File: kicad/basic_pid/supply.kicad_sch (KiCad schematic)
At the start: 0 parts

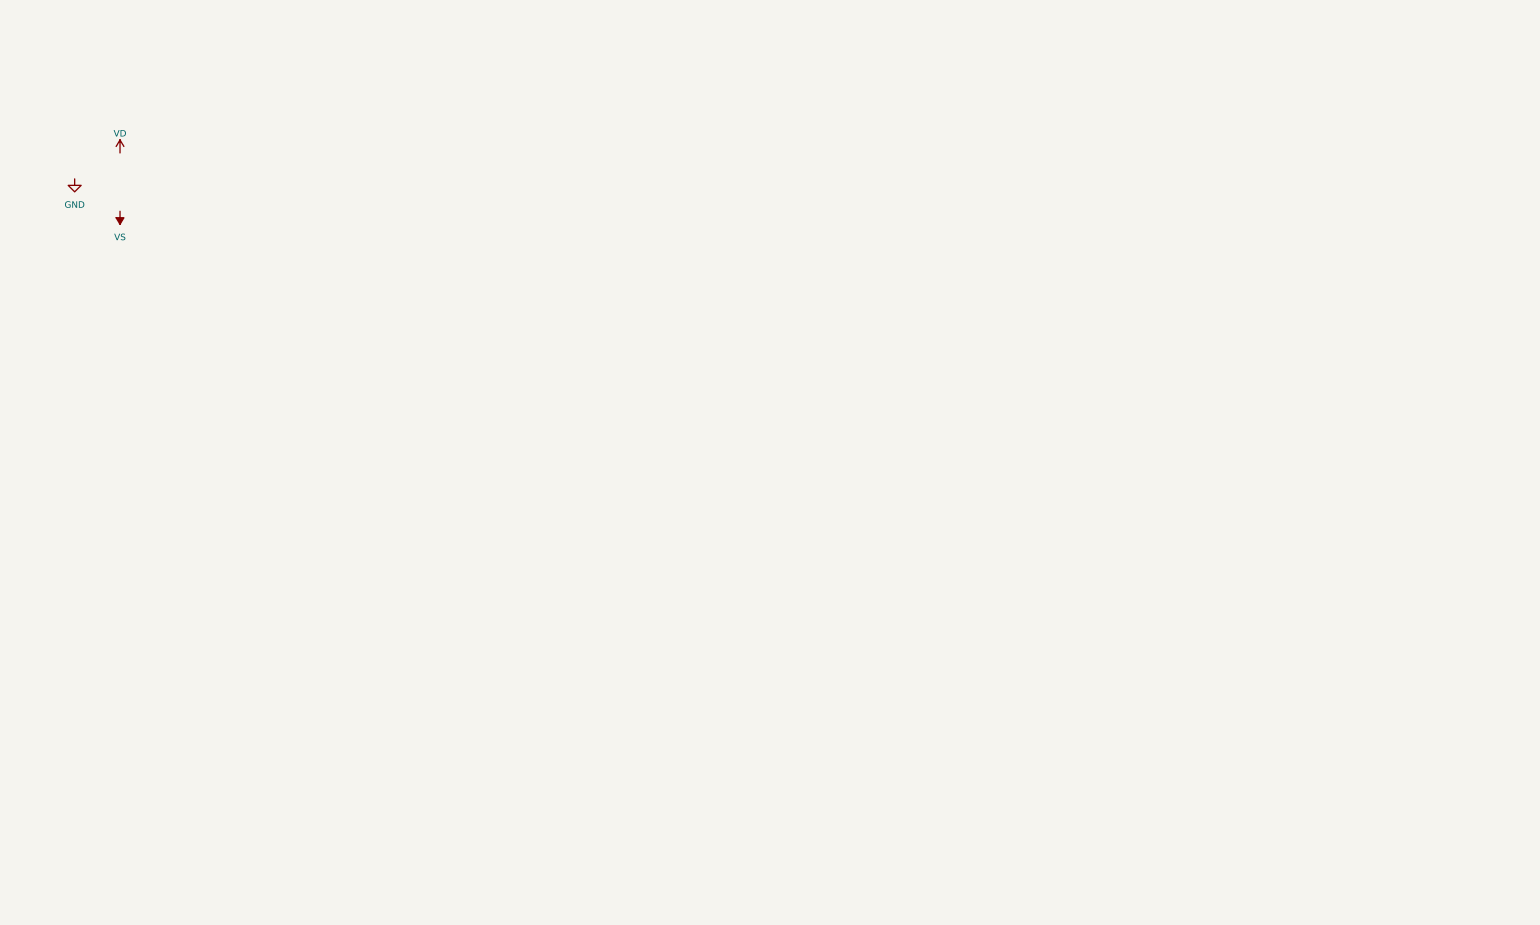
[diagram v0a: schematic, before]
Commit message: Schematic almost finalized:
Ended up using switches to select pre-set capacitors rather than ZIFs

TO DO:
1) design the power supply and filtering section.
2) Layout work (consider adding capacitors for stabilization...)
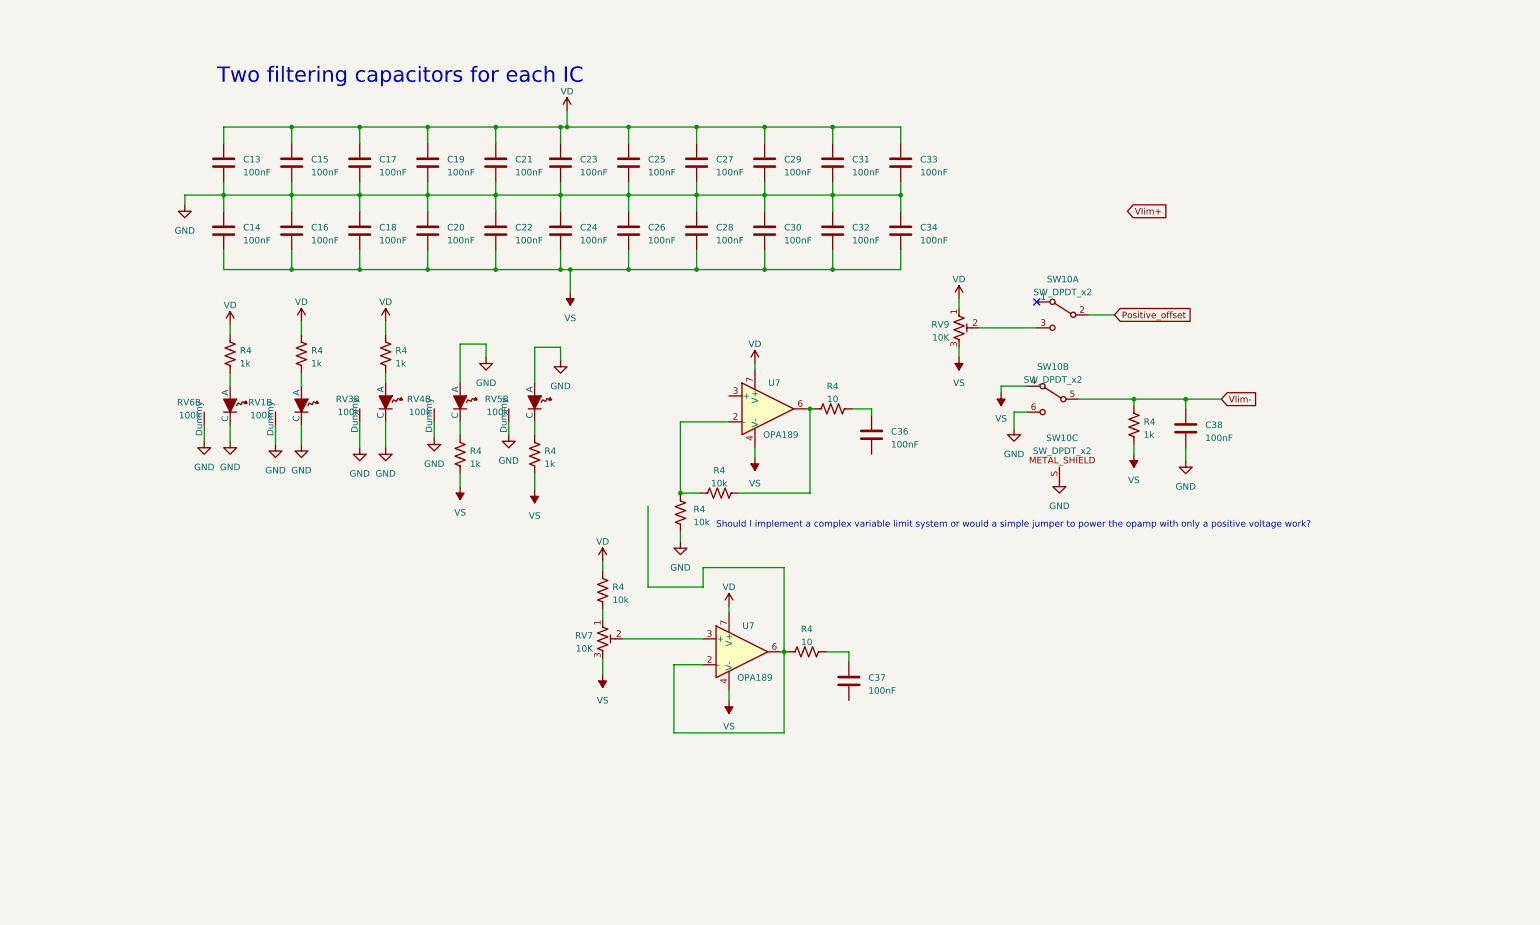
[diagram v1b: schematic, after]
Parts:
- added C13, C14, C15, C16, C17, C18, C19, C20, C21, C22, C23, C24, C25, C26, C27, C28, C29, C30, C31, C32, C33, C34, C36, C37, C38: 100nF, Capacitor_SMD:C_0805_2012Metric, symbol Device:C
- added R4 (x6): 1k, Resistor_SMD:R_0805_2012Metric, symbol Device:R_US
- added R4 (x2): 10, Resistor_SMD:R_0805_2012Metric, symbol Device:R_US
- added R4 (x3): 10k, Resistor_SMD:R_0805_2012Metric, symbol Device:R_US
- added RV1, RV3, RV4, RV5, RV6: 100k, lib:Slide_pot_45mm, symbol local_lib:potentiometer_and _LED
- added RV7, RV9: 10K, Potentiometer_THT:Potentiometer_Bourns_3296W_Vertical, symbol Device:R_Potentiometer_Trim_US
- added SW10: SW_DPDT_x2, lib:MHS222, symbol local_lib:SW_DPDT_x2
- added U7 (x2): OPA189, Package_SO:SOIC-8_3.9x4.9mm_P1.27mm, symbol Amplifier_Operational:OPA330xxD
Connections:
- net GND: now also C13.2, C14.1, C15.2, C16.1, C17.2, C18.1, C19.2, C20.1, C21.2, C22.1, C23.2, C24.1, C25.2, C26.1, C27.2, C28.1, C29.2, C30.1, C31.2, C32.1, C33.2, C34.1, C38.2, R4.2, RV1.C, RV1.L (Dummy), RV3.C, RV3.L (Dummy), RV4.A, RV4.L (Dummy), RV5.A, RV5.L (Dummy), RV6.C, RV6.L (Dummy), SW10.6 (C), SW10.S
- net VD: now also C13.1, C15.1, C17.1, C19.1, C21.1, C23.1, C25.1, C27.1, C29.1, C31.1, C33.1, R4.1, R4.2, R4.2, R4.2, RV9.1, U7.7 (V+), U7.7 (V+)
- net VS: now also C14.2, C16.2, C18.2, C20.2, C22.2, C24.2, C26.2, C28.2, C30.2, C32.2, C34.2, R4.1, R4.1, R4.1, RV7.3, RV9.3, SW10.4 (A), U7.4 (V-), U7.4 (V-)
- new net: R4.1, RV6.A
- new net: R4.2, U7.2 (-), U7.6
- new net: RV7.2, U7.3 (+)
- new net: C36.1, R4.1
- new net: R4.1, R4.2, U7.6
- new net: R4.2, RV7.1
- new net: R4.1, R4.2, U7.2 (-)
- new net: R4.2, RV4.C
- new net: R4.1, RV3.A
- new net: RV9.2, SW10.3 (C)
- new net: C37.1, R4.1
- new net: R4.1, RV1.A
- new net: R4.2, RV5.C
- new net Positive_offset: SW10.2 (B)
- new net Vlim-: C38.1, R4.2, SW10.5 (B)
- no-connect marks 0 -> 1
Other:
- note added: "Should I implement a complex variable limit system or would a simple jumper to power the opamp with only a positive voltage work?"
- note added: "Two filtering capacitors for each IC"

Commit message: last partial schematic using OPA189 everywhere
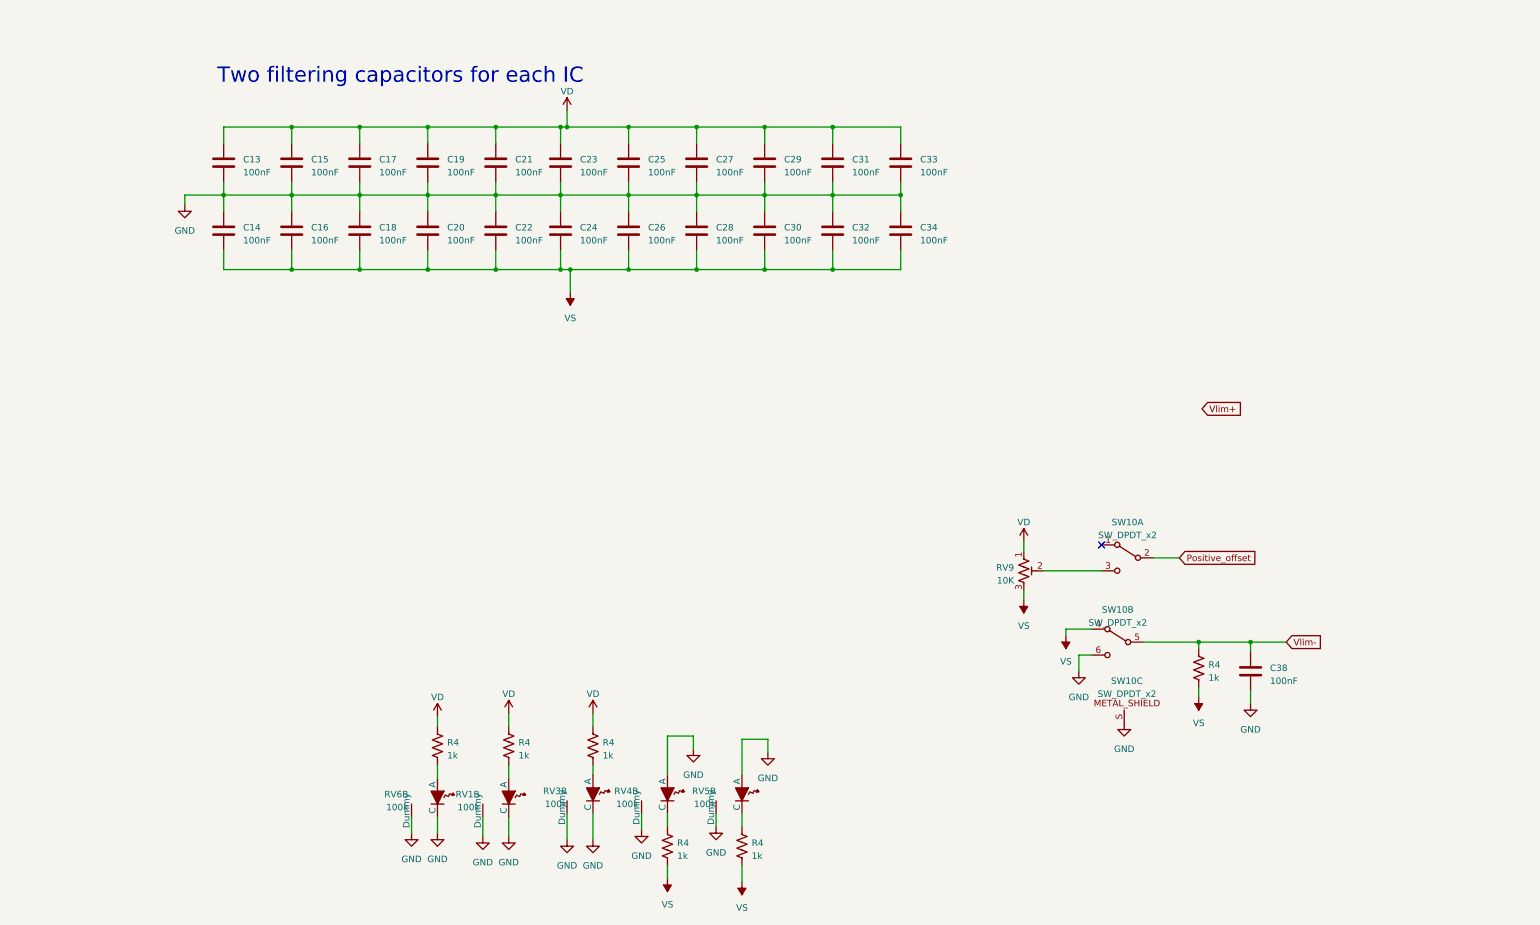
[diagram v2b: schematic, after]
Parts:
- removed C36, C37: 100nF, Capacitor_SMD:C_0805_2012Metric, symbol Device:C
- removed R4 (x2): 10, Resistor_SMD:R_0805_2012Metric, symbol Device:R_US
- removed R4 (x3): 10k, Resistor_SMD:R_0805_2012Metric, symbol Device:R_US
- removed RV7: 10K, Potentiometer_THT:Potentiometer_Bourns_3296W_Vertical, symbol Device:R_Potentiometer_Trim_US
- removed U7 (x2): OPA189, Package_SO:SOIC-8_3.9x4.9mm_P1.27mm, symbol Amplifier_Operational:OPA330xxD
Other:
- note removed: "Should I implement a complex variable limit system or would a simple jumper to power the opamp with only a positive voltage work?"
- moved on the sheet: C38, R4, RV1B, RV3B, RV4B, RV5B, RV6B, RV9, SW10A, SW10B, SW10C

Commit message: Schematic finalized and layout work begun
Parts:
- added C18, C19: 22mF, Capacitor_THT:CP_Radial_D30.0mm_P10.00mm_SnapIn, symbol Device:C_Polarized
- added C24, C25, C42: 10uF, Capacitor_SMD:C_1210_3225Metric, symbol Device:C
- added C32, C33: 220uF, Capacitor_SMD:CP_Elec_8x6.9, symbol Device:C_Polarized
- added C44: 22uF, Capacitor_SMD:CP_Elec_4x5.8, symbol Device:C_Polarized
- added D1: GBU4A, Diode_THT:Diode_Bridge_Vishay_GBU, symbol Diode_Bridge:GBU4A
- added H1, H2, H3, H4: MountingHole, MountingHole:MountingHole_3.2mm_M3_ISO14580, symbol Mechanical:MountingHole
- added J5: Screw_Terminal_01x04, TerminalBlock:TerminalBlock_Altech_AK300-4_P5.00mm, symbol Connector:Screw_Terminal_01x04
- added J6: Screw_Terminal_01x03, TerminalBlock:TerminalBlock_Altech_AK300-3_P5.00mm, symbol Connector:Screw_Terminal_01x03
- added R4: DNP, Resistor_SMD:R_0805_2012Metric, symbol Device:R_US
- added R4: 1k, Resistor_SMD:R_0805_2012Metric, symbol Device:R_US
- added R4: 330, Resistor_SMD:R_0805_2012Metric, symbol Device:R_US
- added RV7: 2k, Potentiometer_THT:Potentiometer_Bourns_3296W_Vertical, symbol Device:R_Potentiometer_Trim_US
- added SW1, SW2, SW3, SW5: SW_DPDT_x2, lib:MHS222, symbol local_lib:SW_DPDT_x2
- added U14: LM2940CS-12/NOPB, Package_TO_SOT_SMD:TO-263-3_TabPin2, symbol Regulator_Linear:LM2937xS
- added U15: LM2990SX-12, Package_TO_SOT_SMD:TO-263-3_TabPin2, symbol Regulator_Linear:LM2990SX-12
- added U16: LM317_TO-252, Package_TO_SOT_SMD:TO-252-2, symbol Regulator_Linear:LM317_TO-252
- RV6: renamed from RV9; DIGIKEY (none) -> 118-3296W-1-103RLFCT-ND; PARTNO (none) -> 3296W-1-103RLF
- renumbered C13 to C14, C14 to C15, C15 to C16, C16 to C17, C17 to C20, C18 to C21, C19 to C22, C20 to C23, C21 to C26, C22 to C27, C23 to C28, C24 to C29, C25 to C30, C26 to C31, C27 to C34, C28 to C35, C29 to C36, C30 to C37, C31 to C38, C32 to C39, C33 to C40, C34 to C41, C38 to C43
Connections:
- net GND: now also RV6.1, C18.2, C19.1, C24.2, C25.1, C32.2, C33.1, C42.2, C44.2, J5.2 (Pin_2), J5.3 (Pin_3), J6.2 (Pin_2), RV7.2, RV7.3, SW1.S, SW2.S, SW3.S, SW5.S, U14.2 (GND), U15.1 (GND)
- net Vlim+: now also C44.1, R4.2, U16.2 (VO)
- net at RV6.2, SW10.3 (C): now also R4.2
- net VD renamed +12V
- net +12V: now also C32.1, U14.3 (VO); no longer RV6.1
- net VS renamed -12V
- net -12V: now also C33.2, R4.1, U15.3 (OUT)
- new net: C19.2, C25.2, D1.4 (-), J6.3 (Pin_3), U15.2 (IN)
- new net: D1.3, J5.1 (Pin_1)
- new net: D1.2, J5.4 (Pin_4)
- new net: R4.1, RV7.1
- new net: R4.1, R4.2, U16.1 (ADJ)
- new net V+_unreg: C18.1, C24.1, C42.1, D1.1 (+), J6.1 (Pin_1), U14.1 (VI), U16.3 (VI)
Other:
- note added: "Additional parts: 237-1326-ND VPT30-830 (toroidal transformer) 1144-1033-ND 06AE2 (Power Entry Module)"
- moved on the sheet: C43, R4, RV1B, RV3B, RV6, RV6B, SW10A, SW10B, SW10C

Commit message: Layout almost completed
This is an almost completed snapshot of the layout. Here what to do:

1) Make sure that when flipped the back has sliders on the bottom: this will require
   reversing the direction of increasing gain with consequent shortening of certain
   signal traces

2) Fix the position of connectors, sliders and switches to "reasonable locations"
3) Make a verbose silkscreen (expecially on bottom) showing all functions.
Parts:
- removed C41: 100nF, Capacitor_SMD:C_0805_2012Metric, symbol Device:C
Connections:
- net +12V: no longer C40.1
- net V+_unreg: now also J6.3 (Pin_3); no longer J6.1 (Pin_1)
- net Vlim+: now also C40.1
- net at C19.2, C25.2, D1.4 (-)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: now also J6.1 (Pin_1); no longer J6.3 (Pin_3)
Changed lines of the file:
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@@
   (junction (at 109.22 66.04) (diameter 0) (color 0 0 0 0)
   )
-  (junction (at 175.26 38.1) (diameter 0) (color 0 0 0 0)
-  )
   (junction (at 223.52 88.265) (diameter 0) (color 0 0 0 0)
   )
@@
   (junction (at 211.455 74.295) (diameter 0) (color 0 0 0 0)
   )
-  (junction (at 175.26 66.04) (diameter 0) (color 0 0 0 0)
-  )
   (junction (at 78.105 110.49) (diameter 0) (color 0 0 0 0)
   )
+  (junction (at 257.81 74.295) (diameter 0) (color 0 0 0 0)
+  )
   (junction (at 108.585 137.795) (diameter 0) (color 0 0 0 0)
   )
@@
   (junction (at 236.22 74.295) (diameter 0) (color 0 0 0 0)
   )
-  (junction (at 188.595 51.435) (diameter 0) (color 0 0 0 0)
-  )
   (junction (at 135.255 66.04) (diameter 0) (color 0 0 0 0)
   )
@@
     (stroke (width 0) (type default))
   )
-  (wire (pts (xy 188.595 51.435) (xy 188.595 54.61))
-    (stroke (width 0) (type default))
-  )
   (wire (pts (xy 69.215 51.435) (xy 69.215 54.61))
     (stroke (width 0) (type default))
@@
     (stroke (width 0) (type default))
   )
-  (wire (pts (xy 188.595 38.1) (xy 175.26 38.1))
-    (stroke (width 0) (type default))
-  )
-  (wire (pts (xy 188.595 66.04) (xy 188.595 62.23))
-    (stroke (width 0) (type default))
-  )
   (wire (pts (xy 55.88 41.275) (xy 55.88 38.1))
     (stroke (width 0) (type default))
@@
     (stroke (width 0) (type default))
   )
-  (wire (pts (xy 175.26 66.04) (xy 188.595 66.04))
+  (wire (pts (xy 257.81 74.295) (xy 257.81 77.47))
     (stroke (width 0) (type default))
   )
@@
     (stroke (width 0) (type default))
   )
-  (wire (pts (xy 188.595 48.895) (xy 188.595 51.435))
-    (stroke (width 0) (type default))
-  )
   (wire (pts (xy 55.88 51.435) (xy 55.88 54.61))
     (stroke (width 0) (type default))
@@
     (stroke (width 0) (type default))
   )
+  (wire (pts (xy 257.81 74.295) (xy 260.985 74.295))
+    (stroke (width 0) (type default))
+  )
   (wire (pts (xy 35.56 141.605) (xy 67.945 141.605))
     (stroke (width 0) (type default))
@@
     (stroke (width 0) (type default))
   )
+  (wire (pts (xy 257.81 85.09) (xy 257.81 86.36))
+    (stroke (width 0) (type default))
+  )
   (wire (pts (xy 84.455 126.365) (xy 84.455 137.795))
     (stroke (width 0) (type default))
@@
     (stroke (width 0) (type default))
   )
-  (wire (pts (xy 188.595 41.275) (xy 188.595 38.1))
-    (stroke (width 0) (type default))
-  )
   (wire (pts (xy 236.22 88.265) (xy 223.52 88.265))
     (stroke (width 0) (type default))
@@
     (stroke (width 0) (type default))
   )
-  (wire (pts (xy 175.26 51.435) (xy 188.595 51.435))
-    (stroke (width 0) (type default))
-  )
   (wire (pts (xy 135.255 137.795) (xy 135.255 139.7))
     (stroke (width 0) (type default))
@@
     (stroke (width 0) (type default))
   )
-  (wire (pts (xy 246.38 74.295) (xy 260.985 74.295))
+  (wire (pts (xy 246.38 74.295) (xy 257.81 74.295))
     (stroke (width 0) (type default))
   )
@@
     )
   )
-  (symbol (lib_id "Connector:Screw_Terminal_01x03") (at 91.44 123.825 0) (unit 1)
+  (symbol (lib_id "Connector:Screw_Terminal_01x03") (at 91.44 123.825 0) (mirror x) (unit 1)
     (in_bom yes) (on_board yes) (dnp no)
-    (property "Reference" "J6" (at 93.98 123.19 0)
+    (property "Reference" "J6" (at 93.98 124.46 0)
       (effects (font (size 1.27 1.27)) (justify left))
     )
-    (property "Value" "Screw_Terminal_01x03" (at 85.725 128.905 0)
+    (property "Value" "Screw_Terminal_01x03" (at 85.725 118.745 0)
       (effects (font (size 1.27 1.27)) (justify left))
     )
@@
     )
   )
-  (symbol (lib_id "Device:C") (at 188.595 58.42 0) (unit 1)
-    (in_bom yes) (on_board yes) (dnp no) (fields_autoplaced)
-    (property "Reference" "C41" (at 192.405 57.785 0)
-      (effects (font (size 1.27 1.27)) (justify left))
-    )
-    (property "Value" "100nF" (at 192.405 60.325 0)
-      (effects (font (size 1.27 1.27)) (justify left))
-    )
-    (property "Footprint" "Capacitor_SMD:C_0805_2012Metric" (at 189.5602 62.23 0)
-      (effects (font (size 1.27 1.27)) hide)
-    )
-    (property "Datasheet" "~" (at 188.595 58.42 0)
-      (effects (font (size 1.27 1.27)) hide)
-    )
-    (pin "1")
-    (pin "2")
-    (instances
-      (project "basic_pid"
-        (path "/3a3d7bcb-6fa5-41ef-9ea1-6d4ab7c492fd/a04c5785-e230-4149-bf27-97ee4701c201"
-          (reference "C41") (unit 1)
-        )
-      )
-    )
-  )
   (symbol (lib_id "Device:C") (at 82.55 45.085 0) (unit 1)
     (in_bom yes) (on_board yes) (dnp no) (fields_autoplaced)
@@
     )
   )
+  (symbol (lib_id "power:GND") (at 257.81 86.36 0) (unit 1)
+    (in_bom yes) (on_board yes) (dnp no) (fields_autoplaced)
+    (property "Reference" "#PWR076" (at 257.81 92.71 0)
+      (effects (font (size 1.27 1.27)) hide)
+    )
+    (property "Value" "GND" (at 257.81 90.805 0)
+      (effects (font (size 1.27 1.27)))
+    )
+    (property "Footprint" "" (at 257.81 86.36 0)
+      (effects (font (size 1.27 1.27)) hide)
+    )
+    (property "Datasheet" "" (at 257.81 86.36 0)
+      (effects (font (size 1.27 1.27)) hide)
+    )
+    (pin "1")
+    (instances
+      (project "basic_pid"
+        (path "/3a3d7bcb-6fa5-41ef-9ea1-6d4ab7c492fd/a04c5785-e230-4149-bf27-97ee4701c201"
+          (reference "#PWR076") (unit 1)
+        )
+      )
+    )
+  )
   (symbol (lib_id "power:GND") (at 204.47 146.05 0) (unit 1)
     (in_bom yes) (on_board yes) (dnp no) (fields_autoplaced)
@@
     )
   )
-  (symbol (lib_id "Device:C") (at 188.595 45.085 0) (unit 1)
-    (in_bom yes) (on_board yes) (dnp no) (fields_autoplaced)
-    (property "Reference" "C40" (at 192.405 44.45 0)
-      (effects (font (size 1.27 1.27)) (justify left))
-    )
-    (property "Value" "100nF" (at 192.405 46.99 0)
-      (effects (font (size 1.27 1.27)) (justify left))
-    )
-    (property "Footprint" "Capacitor_SMD:C_0805_2012Metric" (at 189.5602 48.895 0)
-      (effects (font (size 1.27 1.27)) hide)
-    )
-    (property "Datasheet" "~" (at 188.595 45.085 0)
-      (effects (font (size 1.27 1.27)) hide)
-    )
-    (pin "1")
-    (pin "2")
-    (instances
-      (project "basic_pid"
-        (path "/3a3d7bcb-6fa5-41ef-9ea1-6d4ab7c492fd/a04c5785-e230-4149-bf27-97ee4701c201"
-          (reference "C40") (unit 1)
-        )
-      )
-    )
-  )
   (symbol (lib_id "Regulator_Linear:LM317_TO-252") (at 223.52 74.295 0) (unit 1)
     (in_bom yes) (on_board yes) (dnp no) (fields_autoplaced)
@@
         )
       )
+    )
+  )
+  (symbol (lib_id "Device:C") (at 257.81 81.28 0) (unit 1)
+    (in_bom yes) (on_board yes) (dnp no) (fields_autoplaced)
+    (property "Reference" "C40" (at 261.62 80.645 0)
+      (effects (font (size 1.27 1.27)) (justify left))
+    )
+    (property "Value" "100nF" (at 261.62 83.185 0)
+      (effects (font (size 1.27 1.27)) (justify left))
+    )
+    (property "Footprint" "Capacitor_SMD:C_0805_2012Metric" (at 258.7752 85.09 0)
+      (effects (font (size 1.27 1.27)) hide)
+    )
+    (property "Datasheet" "~" (at 257.81 81.28 0)
+      (effects (font (size 1.27 1.27)) hide)
+    )
+    (pin "1")
+    (pin "2")
+    (instances
+      (project "basic_pid"
+        (path "/3a3d7bcb-6fa5-41ef-9ea1-6d4ab7c492fd/a04c5785-e230-4149-bf27-97ee4701c201"
+          (reference "C40") (unit 1)
+        )
+      )
